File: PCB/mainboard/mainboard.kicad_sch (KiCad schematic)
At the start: 1 part

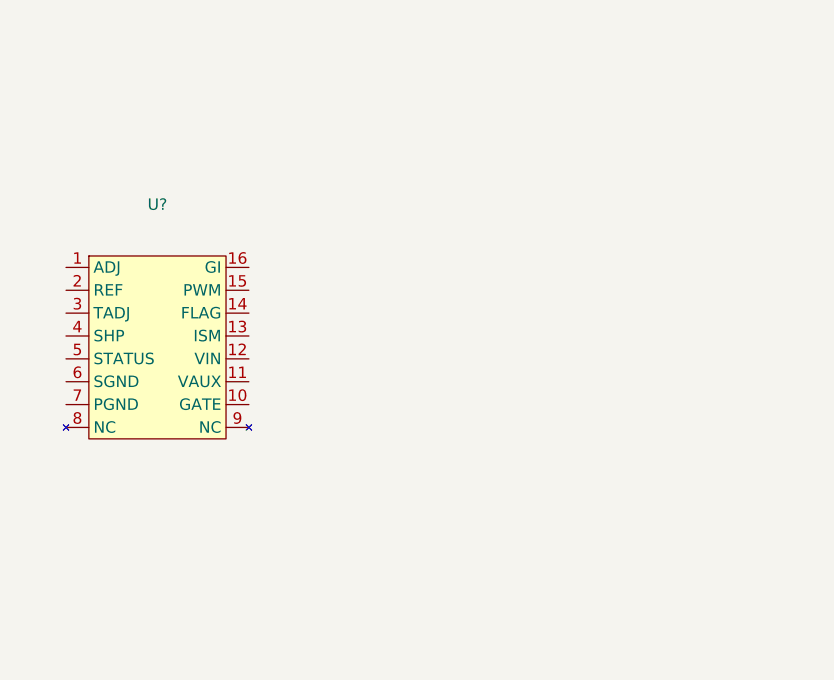
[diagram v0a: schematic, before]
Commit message: fix symboland add more components
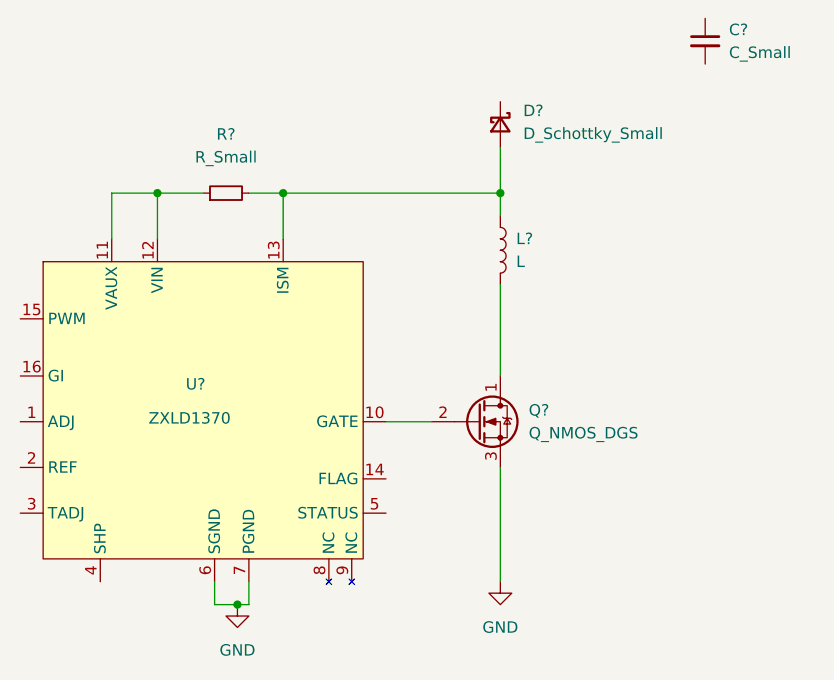
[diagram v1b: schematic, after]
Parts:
- added C?: C_Small, symbol Device:C_Small
- added D?: D_Schottky_Small, symbol Device:D_Schottky_Small
- added L?: L, symbol Device:L
- added Q?: Q_NMOS_DGS, symbol Device:Q_NMOS_DGS
- added R?: R_Small, symbol Device:R_Small
- U?: value (none) -> ZXLD1370
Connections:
- net at U?.10 (GATE): now also Q?.2 (G)
- net at U?.11 (VAUX): now also U?.12 (VIN), R?.1
- net at U?.13 (ISM): now also D?.2 (A), L?.1, R?.2
- net GND: now reaches U?.6 (SGND)
- net GND: now also U?.7 (PGND), Q?.3 (S)
- new net: L?.2, Q?.1 (D)
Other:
- moved on the sheet: U?
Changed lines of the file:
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@@
 (kicad_sch (version 20211123) (generator eeschema)
   (paper "A4")
-  (symbol (lib_id "photon_components:ZXLD1370") (at 104.14 67.945 0) (unit 1)
-    (in_bom yes) (on_board yes) (fields_autoplaced)
-    (property "Reference" "U?" (id 0) (at 104.14 57.15 0))
-    (property "Value" "" (id 1) (at 104.14 59.69 0))
-    (property "Footprint" "" (id 2) (at 101.6 67.945 0)
-      (effects (font (size 1.27 1.27)) hide)
-    )
-    (property "Datasheet" "" (id 3) (at 101.6 67.945 0)
+  (junction (at 142.24 55.88) (diameter 0) (color 0 0 0 0)
+  )
+  (junction (at 113.03 101.6) (diameter 0) (color 0 0 0 0)
+  )
+  (junction (at 104.14 55.88) (diameter 0) (color 0 0 0 0)
+  )
+  (junction (at 118.11 55.88) (diameter 0) (color 0 0 0 0)
+  )
+  (wire (pts (xy 118.11 55.88) (xy 118.11 60.96))
+    (stroke (width 0) (type default) (color 0 0 0 0))
+  )
+  (wire (pts (xy 110.49 99.06) (xy 110.49 101.6))
+    (stroke (width 0) (type default) (color 0 0 0 0))
+  )
+  (wire (pts (xy 113.03 101.6) (xy 114.3 101.6))
+    (stroke (width 0) (type default) (color 0 0 0 0))
+  )
+  (wire (pts (xy 104.14 60.96) (xy 104.14 55.88))
+    (stroke (width 0) (type default) (color 0 0 0 0))
+  )
+  (wire (pts (xy 142.24 86.36) (xy 142.24 99.06))
+    (stroke (width 0) (type default) (color 0 0 0 0))
+  )
+  (wire (pts (xy 142.24 66.04) (xy 142.24 76.2))
+    (stroke (width 0) (type default) (color 0 0 0 0))
+  )
+  (wire (pts (xy 104.14 55.88) (xy 109.22 55.88))
+    (stroke (width 0) (type default) (color 0 0 0 0))
+  )
+  (wire (pts (xy 114.3 55.88) (xy 118.11 55.88))
+    (stroke (width 0) (type default) (color 0 0 0 0))
+  )
+  (wire (pts (xy 99.06 60.96) (xy 99.06 55.88))
+    (stroke (width 0) (type default) (color 0 0 0 0))
+  )
+  (wire (pts (xy 99.06 55.88) (xy 104.14 55.88))
+    (stroke (width 0) (type default) (color 0 0 0 0))
+  )
+  (wire (pts (xy 142.24 50.8) (xy 142.24 55.88))
+    (stroke (width 0) (type default) (color 0 0 0 0))
+  )
+  (wire (pts (xy 118.11 55.88) (xy 142.24 55.88))
+    (stroke (width 0) (type default) (color 0 0 0 0))
+  )
+  (wire (pts (xy 114.3 101.6) (xy 114.3 99.06))
+    (stroke (width 0) (type default) (color 0 0 0 0))
+  )
+  (wire (pts (xy 142.24 58.42) (xy 142.24 55.88))
+    (stroke (width 0) (type default) (color 0 0 0 0))
+  )
+  (wire (pts (xy 110.49 101.6) (xy 113.03 101.6))
+    (stroke (width 0) (type default) (color 0 0 0 0))
+  )
+  (wire (pts (xy 129.54 81.28) (xy 134.62 81.28))
+    (stroke (width 0) (type default) (color 0 0 0 0))
+  )
+  (symbol (lib_id "Device:D_Schottky_Small") (at 142.24 48.26 270) (unit 1)
+    (in_bom yes) (on_board yes) (fields_autoplaced)
+    (property "Reference" "D?" (id 0) (at 144.78 46.7359 90)
+      (effects (font (size 1.27 1.27)) (justify left))
+    )
+    (property "Value" "D_Schottky_Small" (id 1) (at 144.78 49.2759 90)
+      (effects (font (size 1.27 1.27)) (justify left))
+    )
+    (property "Footprint" "" (id 2) (at 142.24 48.26 90)
+      (effects (font (size 1.27 1.27)) hide)
+    )
+    (property "Datasheet" "~" (id 3) (at 142.24 48.26 90)
+      (effects (font (size 1.27 1.27)) hide)
+    )
+    (pin "1")
+    (pin "2")
+  )
+  (symbol (lib_id "Device:R_Small") (at 111.76 55.88 90) (unit 1)
+    (in_bom yes) (on_board yes) (fields_autoplaced)
+    (property "Reference" "R?" (id 0) (at 111.76 49.3522 90))
+    (property "Value" "R_Small" (id 1) (at 111.76 51.8922 90))
+    (property "Footprint" "" (id 2) (at 111.76 55.88 0)
+      (effects (font (size 1.27 1.27)) hide)
+    )
+    (property "Datasheet" "~" (id 3) (at 111.76 55.88 0)
+      (effects (font (size 1.27 1.27)) hide)
+    )
+    (pin "1")
+    (pin "2")
+  )
+  (symbol (lib_id "power:GND") (at 142.24 99.06 0) (unit 1)
+    (in_bom yes) (on_board yes) (fields_autoplaced)
+    (property "Reference" "#PWR?" (id 0) (at 142.24 105.41 0)
+      (effects (font (size 1.27 1.27)) hide)
+    )
+    (property "Value" "GND" (id 1) (at 142.24 104.14 0))
+    (property "Footprint" "" (id 2) (at 142.24 99.06 0)
+      (effects (font (size 1.27 1.27)) hide)
+    )
+    (property "Datasheet" "" (id 3) (at 142.24 99.06 0)
+      (effects (font (size 1.27 1.27)) hide)
+    )
+    (pin "1")
+  )
+  (symbol (lib_id "Device:C_Small") (at 165 39 0) (unit 1)
+    (in_bom yes) (on_board yes) (fields_autoplaced)
+    (property "Reference" "C?" (id 0) (at 167.6416 37.7362 0)
+      (effects (font (size 1.27 1.27)) (justify left))
+    )
+    (property "Value" "C_Small" (id 1) (at 167.6416 40.2762 0)
+      (effects (font (size 1.27 1.27)) (justify left))
+    )
+    (property "Footprint" "" (id 2) (at 165 39 0)
+      (effects (font (size 1.27 1.27)) hide)
+    )
+    (property "Datasheet" "~" (id 3) (at 165 39 0)
+      (effects (font (size 1.27 1.27)) hide)
+    )
+    (pin "1")
+    (pin "2")
+  )
+  (symbol (lib_id "Device:L") (at 142.24 62.23 0) (unit 1)
+    (in_bom yes) (on_board yes) (fields_autoplaced)
+    (property "Reference" "L?" (id 0) (at 143.9926 60.9599 0)
+      (effects (font (size 1.27 1.27)) (justify left))
+    )
+    (property "Value" "L" (id 1) (at 143.9926 63.4999 0)
+      (effects (font (size 1.27 1.27)) (justify left))
+    )
+    (property "Footprint" "" (id 2) (at 142.24 62.23 0)
+      (effects (font (size 1.27 1.27)) hide)
+    )
+    (property "Datasheet" "~" (id 3) (at 142.24 62.23 0)
+      (effects (font (size 1.27 1.27)) hide)
+    )
+    (pin "1")
+    (pin "2")
+  )
+  (symbol (lib_id "photon_components:ZXLD1370") (at 99.06 68.58 0) (unit 1)
+    (in_bom yes) (on_board yes)
+    (property "Reference" "U?" (id 0) (at 108.3818 77.1144 0))
+    (property "Value" "ZXLD1370" (id 1) (at 107.7214 80.899 0))
+    (property "Footprint" "" (id 2) (at 96.52 68.58 0)
+      (effects (font (size 1.27 1.27)) hide)
+    )
+    (property "Datasheet" "" (id 3) (at 96.52 68.58 0)
       (effects (font (size 1.27 1.27)) hide)
     )
@@
     (pin "9")
   )
+  (symbol (lib_id "Device:Q_NMOS_DGS") (at 139.7 81.28 0) (unit 1)
+    (in_bom yes) (on_board yes) (fields_autoplaced)
+    (property "Reference" "Q?" (id 0) (at 145.3896 80.0099 0)
+      (effects (font (size 1.27 1.27)) (justify left))
+    )
+    (property "Value" "Q_NMOS_DGS" (id 1) (at 145.3896 82.5499 0)
+      (effects (font (size 1.27 1.27)) (justify left))
+    )
+    (property "Footprint" "" (id 2) (at 144.78 78.74 0)
+      (effects (font (size 1.27 1.27)) hide)
+    )
+    (property "Datasheet" "~" (id 3) (at 139.7 81.28 0)
+      (effects (font (size 1.27 1.27)) hide)
+    )
+    (pin "1")
+    (pin "2")
+    (pin "3")
+  )
+  (symbol (lib_id "power:GND") (at 113.03 101.6 0) (unit 1)
+    (in_bom yes) (on_board yes) (fields_autoplaced)
+    (property "Reference" "#PWR?" (id 0) (at 113.03 107.95 0)
+      (effects (font (size 1.27 1.27)) hide)
+    )
+    (property "Value" "GND" (id 1) (at 113.03 106.68 0))
+    (property "Footprint" "" (id 2) (at 113.03 101.6 0)
+      (effects (font (size 1.27 1.27)) hide)
+    )
+    (property "Datasheet" "" (id 3) (at 113.03 101.6 0)
+      (effects (font (size 1.27 1.27)) hide)
+    )
+    (pin "1")
+  )
   (sheet_instances
     (path "/" (page "1"))
   )
   (symbol_instances
+    (path "/7e8fac6f-e22f-4856-ae9c-5cb3f6b8ae8b"
+      (reference "#PWR?") (unit 1) (value "GND") (footprint "")
+    )
+    (path "/ed5f58b3-e49e-4639-abd9-9eb3afd6f3e5"
+      (reference "#PWR?") (unit 1) (value "GND") (footprint "")
+    )
+    (path "/90c2bcd7-da8a-4284-bde4-becce0d29e24"
+      (reference "C?") (unit 1) (value "C_Small") (footprint "")
+    )
+    (path "/2e184c6a-ea31-461b-b1fd-f6f04bb9ca93"
+      (reference "D?") (unit 1) (value "D_Schottky_Small") (footprint "")
+    )
+    (path "/a79874a1-1565-4f42-b123-f4b47497c344"
+      (reference "L?") (unit 1) (value "L") (footprint "")
+    )
+    (path "/c3b4607f-0e7d-4bc8-accc-275953670b7f"
+      (reference "Q?") (unit 1) (value "Q_NMOS_DGS") (footprint "")
+    )
+    (path "/648f0900-74a3-41c6-b227-d63f975a0946"
+      (reference "R?") (unit 1) (value "R_Small") (footprint "")
+    )
     (path "/a819facc-4758-49cf-bdf6-087f7aa18482"
       (reference "U?") (unit 1) (value "ZXLD1370") (footprint "")

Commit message: more schematic
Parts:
- removed D?: D_Schottky_Small, symbol Device:D_Schottky_Small
- added C?: C_Small, symbol Device:C_Small
- added C?: (no value), symbol Device:C_Polarized
- added D?: (no value), symbol Device:D_Schottky
- added J? (x2): (no value), symbol Connector_Generic:Conn_01x02
- added R? (x2): R_Small, symbol Device:R_Small
- added R?: (no value), symbol Device:R_Small
- added U?: (no value), symbol Regulator_Linear:LM7805_TO220
- C?: value C_Small -> (none)
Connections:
- net GND: now also C?.2, C?.2, C?.2, J?.1 (Pin_1), J?.2 (Pin_2), R?.2, R?.2
- net at L?.1, R?.2, U?.13 (ISM): now also D?.2 (A)
- net VBATT: now reaches R?.1, U?.11 (VAUX), U?.12 (VIN)
- net VBATT: now also C?.1, J?.2 (Pin_2)
- net at C?.1: now also U?.4 (SHP)
- net at U?.1 (ADJ): now also U?.2 (REF), U?.3 (TADJ), R?.1
- net PWM: now reaches U?.15 (PWM)
- net PWM: now also R?.1
- net at U?.16 (GI): now also R?.1, R?.2
- new net: C?.1, D?.1 (K), J?.1 (Pin_1)
- no-connect marks 0 -> 2
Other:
- moved on the sheet: C?

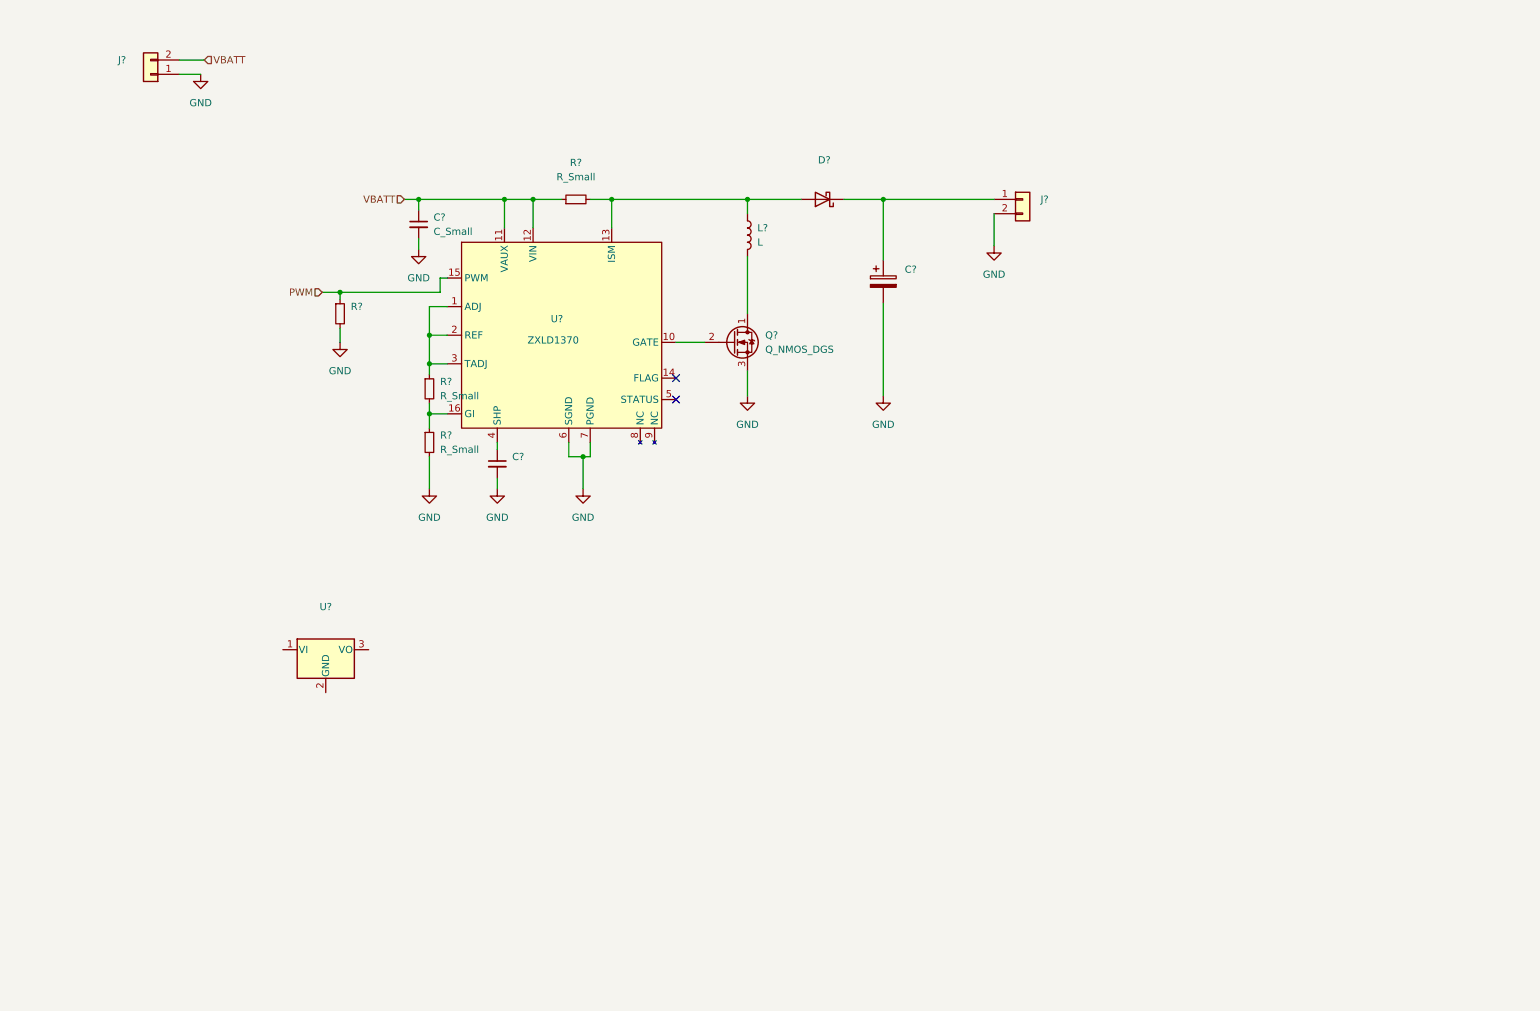
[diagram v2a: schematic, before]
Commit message: add volatage sources
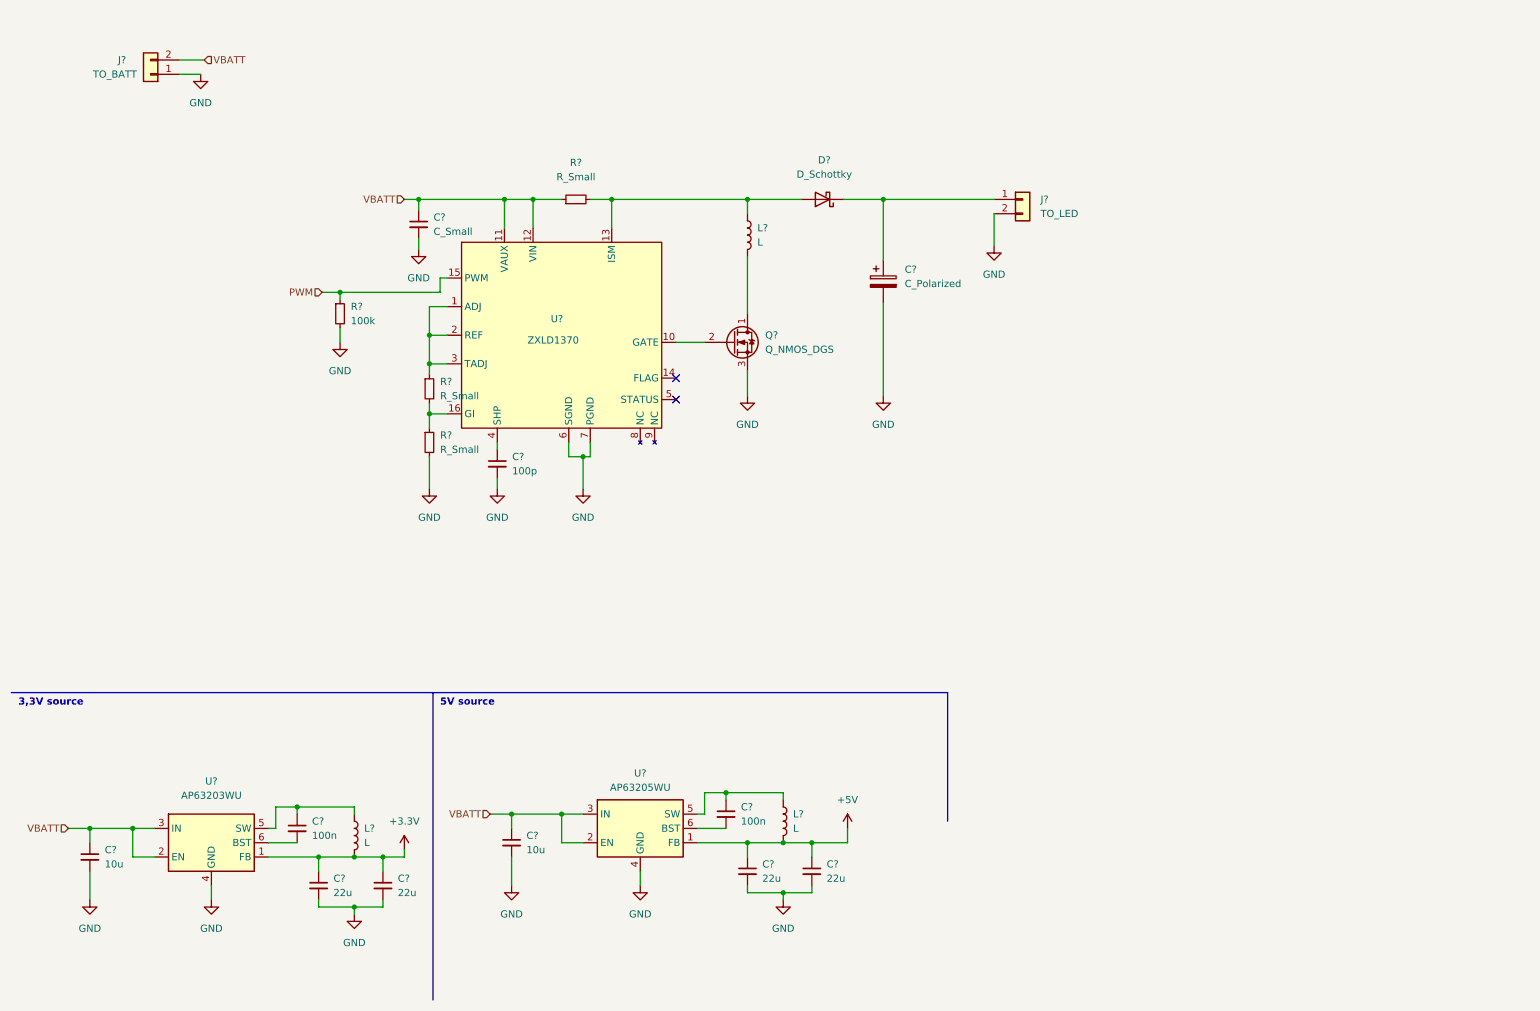
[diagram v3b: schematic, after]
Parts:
- removed U?: (no value), symbol Regulator_Linear:LM7805_TO220
- added C? (x2): 10u, symbol Device:C_Small
- added C? (x2): 100n, symbol Device:C_Small
- added C? (x4): 22u, symbol Device:C_Small
- added L? (x2): L, symbol Device:L
- added U?: AP63205WU, Package_TO_SOT_SMD:TSOT-23-6, symbol Regulator_Switching:AP63205WU
- added U?: AP63203WU, Package_TO_SOT_SMD:TSOT-23-6, symbol Regulator_Switching:AP63203WU
- C?: value (none) -> C_Polarized
- C?: value (none) -> 100p
- D?: value (none) -> D_Schottky
- J?: value (none) -> TO_LED
- J?: value (none) -> TO_BATT
- R?: value (none) -> 100k
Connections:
- net GND: now also C?.2, C?.2, C?.2, C?.2, C?.2, C?.2, U?.4 (GND), U?.4 (GND)
- net VBATT: now also C?.1, C?.1, U?.2 (EN), U?.2 (EN), U?.3 (IN), U?.3 (IN)
- new net: C?.1, L?.1, U?.5 (SW) (x2)
- new net: C?.2, U?.6 (BST) (x2)
- new net +3.3V: C?.1, C?.1, L?.2, U?.1 (FB)
- new net +5V: C?.1, C?.1, L?.2, U?.1 (FB)
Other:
- note added: "3,3V source"
- note added: "5V source"
